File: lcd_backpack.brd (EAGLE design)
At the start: 81.3 x 37.8 mm, 36 parts, among them IC1 LM2936DT-3.0, X1 BU-SMB-V, X2 BU-SMB-V, X3 BU-SMB-V

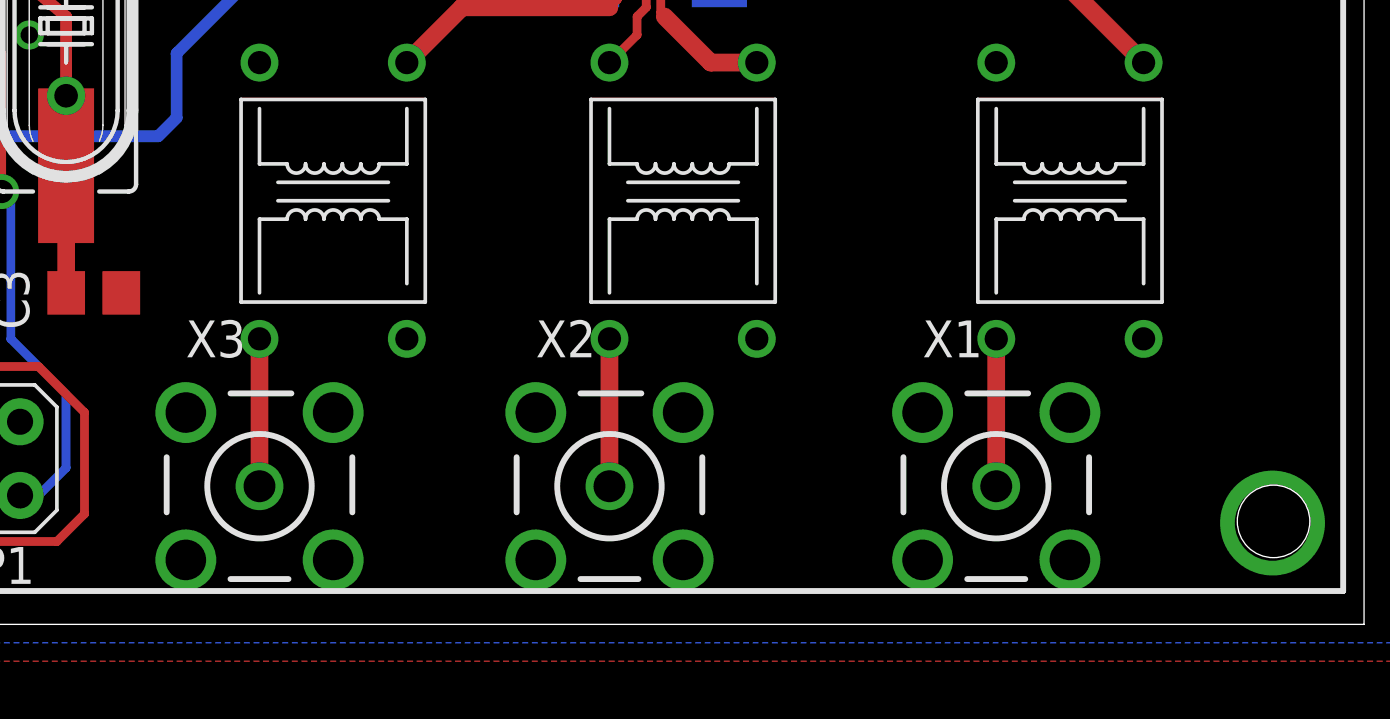
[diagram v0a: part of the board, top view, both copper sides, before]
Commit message: Fixed rendering issue with board
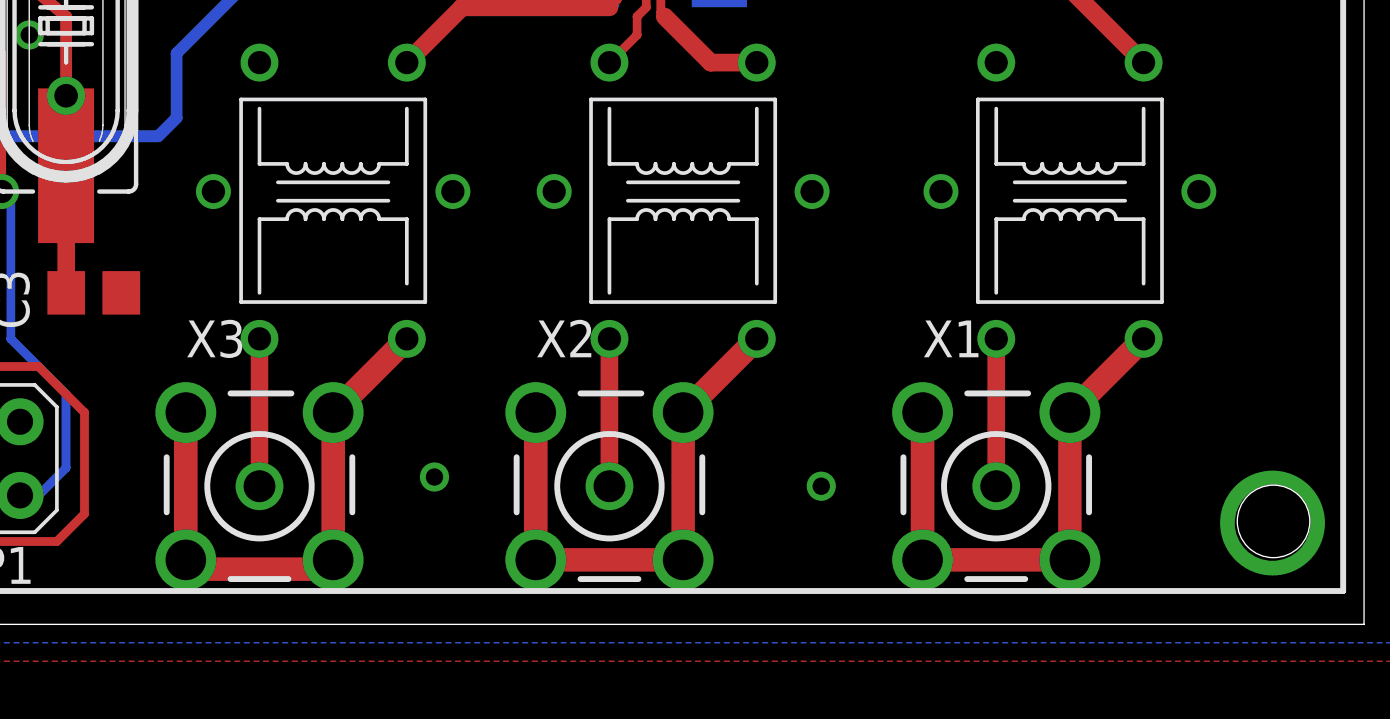
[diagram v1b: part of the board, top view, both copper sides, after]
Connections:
- new net N$35: TR3.P$4, X3.2, X3.3, X3.4, X3.5
- new net N$36: TR2.P$4, X2.2, X2.3, X2.4, X2.5
- new net N$37: TR1.P$4, X1.2, X1.3, X1.4, X1.5
- net GND: no longer TR1.P$4, TR2.P$4, TR3.P$4, X1.2, X1.3, X1.4, X1.5, X2.2, X2.3, X2.4, X2.5, X3.2, X3.3, X3.4, X3.5
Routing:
- net N$36: track 0.00 -> 19.1 mm
- net N$35: track 0.00 -> 19.1 mm
- net N$37: track 0.00 -> 18.8 mm
- net GND: vias 7 -> 9
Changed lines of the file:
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@@
 <contactref element="TR2" pad="P$1"/>
 <contactref element="TR3" pad="P$1"/>
-<contactref element="TR1" pad="P$4"/>
-<contactref element="X1" pad="2"/>
-<contactref element="X1" pad="3"/>
-<contactref element="X1" pad="4"/>
-<contactref element="X1" pad="5"/>
-<contactref element="TR2" pad="P$4"/>
-<contactref element="X2" pad="2"/>
-<contactref element="X2" pad="3"/>
-<contactref element="X2" pad="4"/>
-<contactref element="X2" pad="5"/>
-<contactref element="TR3" pad="P$4"/>
-<contactref element="X3" pad="2"/>
-<contactref element="X3" pad="3"/>
-<contactref element="X3" pad="4"/>
-<contactref element="X3" pad="5"/>
 <contactref element="X4" pad="2"/>
 <contactref element="X4" pad="5"/>
@@
 <via x="25.7175" y="20.0025" extent="1-16" drill="0.6" shape="square"/>
 <via x="35.2425" y="20.32" extent="1-16" drill="0.6" shape="square"/>
+<via x="49.2125" y="5.08" extent="1-16" drill="0.6" shape="square"/>
+<via x="62.5475" y="4.7625" extent="1-16" drill="0.6" shape="square"/>
 </signal>
 <signal name="N$5">
@@
 <wire x1="29.845" y1="3.175" x2="29.845" y2="4.445" width="0.3048" layer="1"/>
 </signal>
+<signal name="N$35">
+<contactref element="TR3" pad="P$4"/>
+<contactref element="X3" pad="2"/>
+<contactref element="X3" pad="3"/>
+<contactref element="X3" pad="4"/>
+<contactref element="X3" pad="5"/>
+<wire x1="45.72" y1="2.2225" x2="45.72" y2="7.3025" width="0.8128" layer="1"/>
+<wire x1="45.72" y1="7.3025" x2="48.26" y2="9.8425" width="0.8128" layer="1"/>
+<wire x1="40.64" y1="7.3025" x2="40.64" y2="2.2225" width="0.8128" layer="1"/>
+<wire x1="40.64" y1="2.2225" x2="40.9575" y2="1.905" width="0.8128" layer="1"/>
+<wire x1="40.9575" y1="1.905" x2="45.4025" y2="1.905" width="0.8128" layer="1"/>
+<wire x1="45.4025" y1="1.905" x2="45.72" y2="2.2225" width="0.8128" layer="1"/>
+</signal>
+<signal name="N$36">
+<contactref element="TR2" pad="P$4"/>
+<contactref element="X2" pad="2"/>
+<contactref element="X2" pad="3"/>
+<contactref element="X2" pad="4"/>
+<contactref element="X2" pad="5"/>
+<wire x1="52.705" y1="7.3025" x2="52.705" y2="2.2225" width="0.8128" layer="1"/>
+<wire x1="57.785" y1="2.2225" x2="58.1025" y2="2.2225" width="0.8128" layer="1"/>
+<wire x1="57.785" y1="2.2225" x2="52.705" y2="2.2225" width="0.8128" layer="1"/>
+<wire x1="57.785" y1="7.3025" x2="57.785" y2="2.2225" width="0.8128" layer="1"/>
+<wire x1="60.325" y1="9.8425" x2="57.785" y2="7.3025" width="0.8128" layer="1"/>
+</signal>
+<signal name="N$37">
+<contactref element="TR1" pad="P$4"/>
+<contactref element="X1" pad="2"/>
+<contactref element="X1" pad="3"/>
+<contactref element="X1" pad="4"/>
+<contactref element="X1" pad="5"/>
+<wire x1="71.12" y1="7.3025" x2="71.12" y2="2.2225" width="0.8128" layer="1"/>
+<wire x1="71.12" y1="7.3025" x2="73.66" y2="9.8425" width="0.8128" layer="1"/>
+<wire x1="66.04" y1="2.2225" x2="71.12" y2="2.2225" width="0.8128" layer="1"/>
+<wire x1="66.04" y1="7.3025" x2="66.04" y2="2.2225" width="0.8128" layer="1"/>
+</signal>
+<signal name="N$38">
+<via x="49.8475" y="14.9225" extent="1-16" drill="0.8"/>
+</signal>
+<signal name="N$39">
+<via x="41.5925" y="14.9225" extent="1-16" drill="0.8"/>
+</signal>
+<signal name="N$40">
+<via x="53.34" y="14.9225" extent="1-16" drill="0.8"/>
+</signal>
+<signal name="N$41">
+<via x="62.23" y="14.9225" extent="1-16" drill="0.8"/>
+</signal>
+<signal name="N$50">
+<via x="66.675" y="14.9225" extent="1-16" drill="0.8"/>
+</signal>
+<signal name="N$51">
+<via x="75.565" y="14.9225" extent="1-16" drill="0.8"/>
+</signal>
 </signals>

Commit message: fixed the USB connector to digikey 609-4618-1-nd
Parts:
- removed CN1: (no value), adafruit:USB-MINIB
- added J1: SMARTPRJ_MYCON2_USB-MINI-B, Arduino_Leonardo-REV3b_lbr:SMARTPRJ_CON2_USB_MICRO_B_AT
- moved C8 7.99 mm to (50.8, 31.1)
- moved C7 7.73 mm to (60.0, 30.5)
- moved Q3 7.73 mm to (55.6, 30.8)
- moved R9 4.62 mm to (18.7, 11.4)
- moved R10 3.27 mm to (22.5, 11.4)
- moved C1 1.59 mm to (26.0, 11.4)
- moved C3 0.95 mm to (36.5, 11.4), turned to 270 degrees
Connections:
- removed net N$35: TR3.P$4, X3.2, X3.3, X3.4, X3.5
- removed net N$36: TR2.P$4, X2.2, X2.3, X2.4, X2.5
- removed net N$37: TR1.P$4, X1.2, X1.3, X1.4, X1.5
- net GND: now also J1.P5, J1.S1, J1.S2, J1.S3, J1.S4, J1.S5, J1.S6, TR1.P$4, TR2.P$4, TR3.P$4, X1.2, X1.3, X1.4, X1.5, X2.2, X2.3, X2.4, X2.5, X3.2, X3.3, X3.4, X3.5; no longer CN1.GND
- net N$1: now also J1.P3, R10.2; no longer CN1.D+, R9.2
- net N$2: now also J1.P2, R9.2; no longer CN1.D-, R10.2
- net N$3: now also J1.P1; no longer CN1.VBUS
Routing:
- net GND: track 3.49 -> 23.1 mm, vias 9 -> 7
- net N$36: track 19.1 -> 0.00 mm
- net N$35: track 19.1 -> 0.00 mm
- net N$37: track 18.8 -> 0.00 mm
- net N$23: track 13.6 -> 7.13 mm
- net N$45: track 8.40 -> 5.70 mm, vias 2 -> 0
- net N$44: track 4.63 -> 6.95 mm
- net N$5: track 3.92 -> 5.71 mm
- net N$3: track 21.2 -> 19.7 mm
- net +3V3: track 147.4 -> 148.4 mm, vias 0 -> 1
- net N$8: track 15.8 -> 14.8 mm
- net N$1: track 4.39 -> 5.16 mm
- net N$22: track 10.6 -> 10.0 mm
- net N$42: track 30.4 -> 31.0 mm

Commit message: connector and via fix. Closed vias.
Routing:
- net N$30: track 29.6 -> 31.5 mm
- net N$42: track 31.0 -> 29.9 mm
- net GND: vias 7 -> 14
